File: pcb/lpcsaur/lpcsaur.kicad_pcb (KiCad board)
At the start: 4 copper layers, 116.8 x 71.1 mm, 157 parts, among them IC1 74LV11, IC2 74LV10, IC3 74HCT08, IC4 74LVC07, IC5 74LVC07, IC6 LM1117-3.3, IC7 LPC1768_TQFP100, J1 X1, J10 LASER, J11 Motor X, J12 Motor Y, J13 Motor Z, J14 Motor AUX, J15 SSR, J16 SSR AUX, J17 RELAY1, J18 V-SELECT, J19 RELAY2, J2 X2, J20 V-SELECT, J21 USB_B, J22 RGB LED, J23 SERIAL, J24 5V IN, J25 12V IN, J26 24V IN, J27 AUX I/O, J28 CHILLER, J29 MICRO-SD, J3 Y1, J4 Y2, J5 Z1, J6 Z2, J7 DOOR1, J8 DOOR2, J9 E-STOP, P0.0 TEST_1P, P0.1 TEST_1P, Q1 ZXMN4A06, Q2 ZXMN4A06, Q3 BSL207SP, Q4 BSL207SP, SW1 SW_PUSH, SW2 SW_PUSH, SW3 SW_PUSH, X1 12 MHz

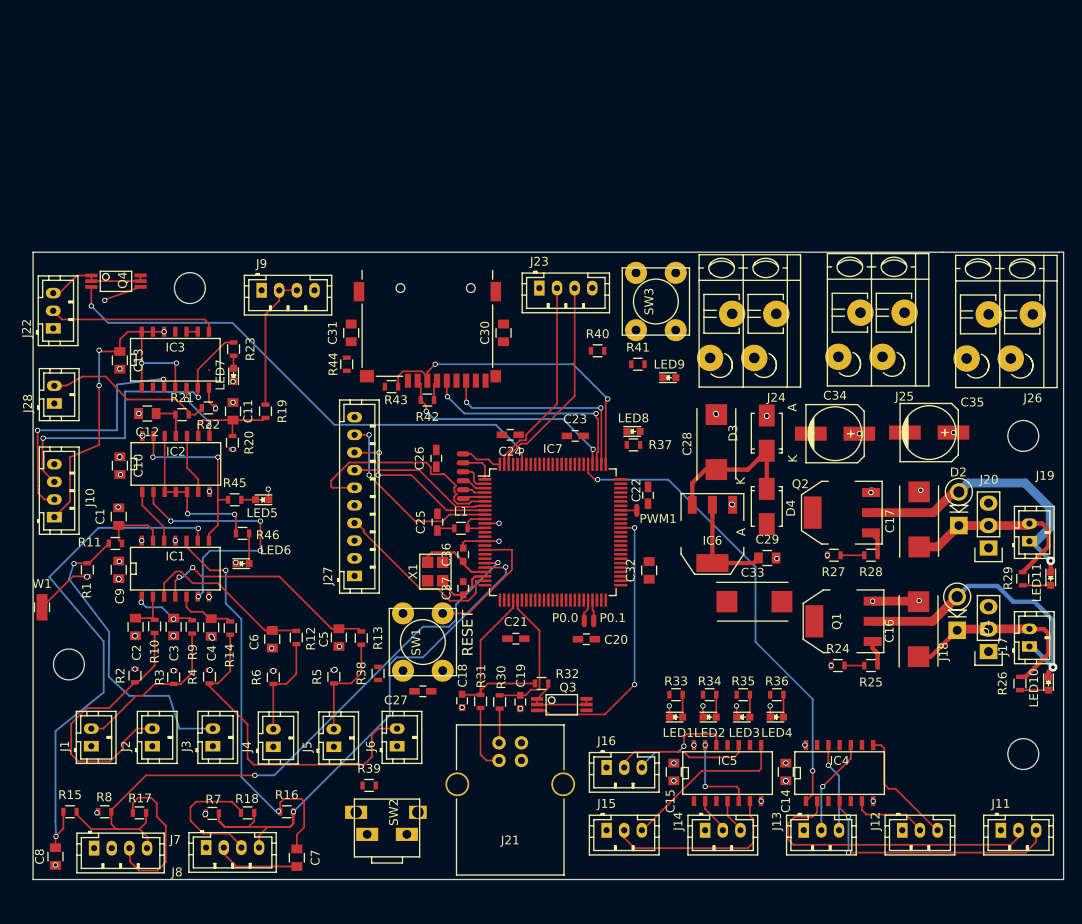
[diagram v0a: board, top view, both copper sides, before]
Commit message: Fix 7410 footprint.
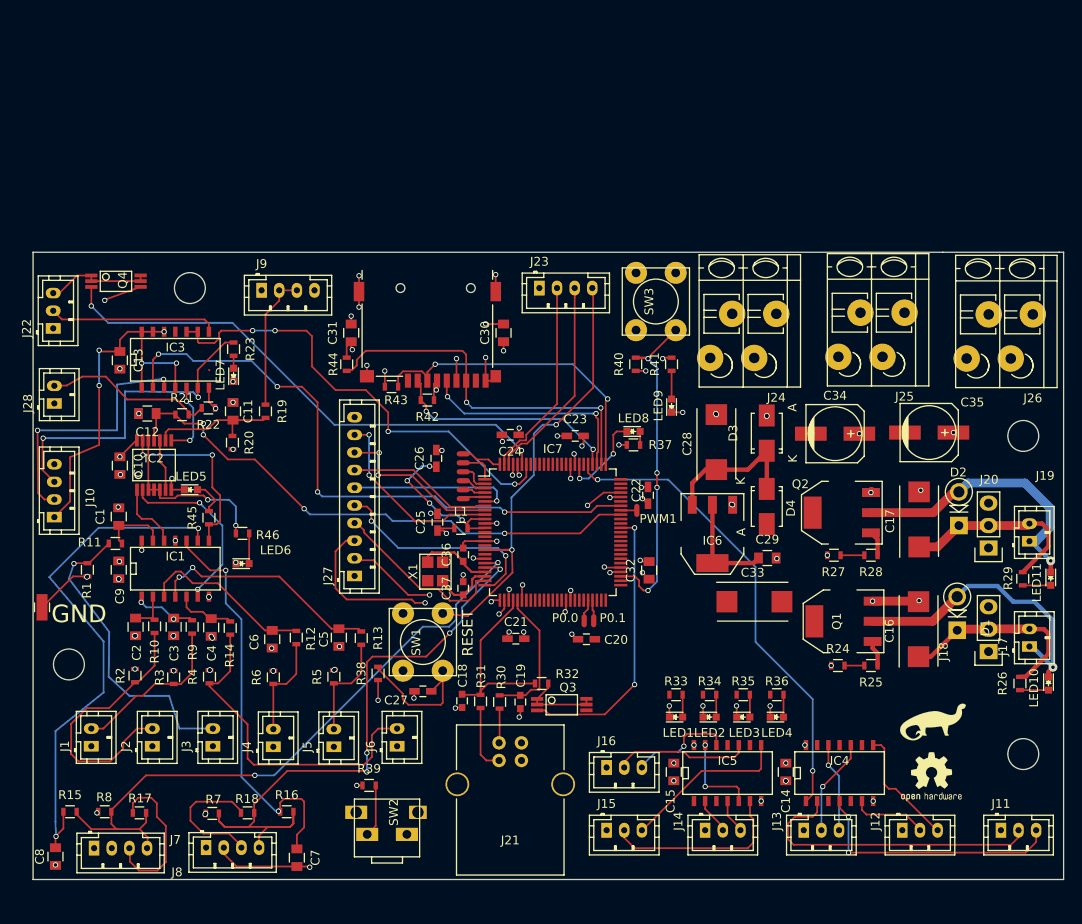
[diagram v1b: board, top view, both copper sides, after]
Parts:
- added G***: LOGO, OPENHARDWARE:OSHWLOGO0.3IN, F.Cu at (186.4, 132.0)
- added G***: LOGO, lpcsaur:dino, F.Cu at (190.1, 129.3)
- IC2: footprint SMD_Packages:SOIC-14_N -> SMD_Packages:SSOP-14
- moved LED5 8.15 mm to (106.3, 103.1), turned to 0 degrees
- moved R40 4.58 mm to (156.7, 88.9), turned to 90 degrees
- moved R41 3.81 mm to (160.8, 88.9), turned to 90 degrees
- moved R45 3.56 mm to (108.3, 106.3), turned to 90 degrees
- moved LED9 3.19 mm to (160.8, 93.6), turned to 90 degrees
- moved IC2 2.49 mm to (102.1, 100.3)
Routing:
- net GND: track 481.3 -> 771.3 mm, vias 63 -> 87
- net +3V3: track 159.4 -> 355.8 mm, vias 12 -> 32
- net +5V: track 140.7 -> 259.1 mm
- net PWM0: track 0.00 -> 70.1 mm, vias 0 -> 4
- net P2.6: track 4.67 -> 63.2 mm, vias 0 -> 4
- net ~RESET: track 15.2 -> 69.4 mm, vias 0 -> 2
- net P1.1: track 1.27 -> 52.9 mm, vias 0 -> 4
- net ~ISP: track 0.00 -> 38.5 mm, vias 0 -> 4
- net Net-(IC7-Pad27): track 0.00 -> 28.7 mm, vias 0 -> 2
- net Net-(IC7-Pad25): track 0.00 -> 25.1 mm, vias 0 -> 2
- net Net-(IC7-Pad26): track 0.00 -> 18.6 mm, vias 0 -> 2
- net SD_MISO: track 24.4 -> 42.4 mm
- net Net-(C26-Pad1): track 4.79 -> 18.1 mm, vias 0 -> 4
- net PLAY_LED: track 0.00 -> 10.4 mm, vias 0 -> 2
- net Net-(IC1-Pad6): track 29.2 -> 20.5 mm, vias 4 -> 2
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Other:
- board text added: "GND"

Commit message: Complete routing.
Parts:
- removed P0.0, P0.1: TEST_1P, lpcsaur2:TP_Oblong
- renumbered Hole2 to Hole4
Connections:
- IC3 pad 11: Net-(IC3-Pad11) -> (no net)
- IC7 pad 13: Net-(IC7-Pad13) -> (no net)
- IC7 pad 14: Net-(IC7-Pad14) -> (no net)
- IC7 pad 16: Net-(IC7-Pad16) -> (no net)
- IC7 pad 18: Net-(IC7-Pad18) -> (no net)
- IC7 pad 46: Net-(IC7-Pad46) -> (no net)
- IC7 pad 47: Net-(IC7-Pad47) -> (no net)
- IC7 pad 48: Net-(IC7-Pad48) -> (no net)
- IC7 pad 50: Net-(IC7-Pad50) -> (no net)
- IC7 pad 52: Net-(IC7-Pad52) -> (no net)
- IC7 pad 57: Net-(IC7-Pad57) -> (no net)
- IC7 pad 62: Net-(IC7-Pad62) -> (no net)
- IC7 pad 65: Net-(IC7-Pad65) -> (no net)
- IC7 pad 66: Net-(IC7-Pad66) -> (no net)
- IC7 pad 81: Net-(IC7-Pad81) -> (no net)
- IC7 pad 85: Net-(IC7-Pad85) -> (no net)
- IC7 pad 86: Net-(IC7-Pad86) -> (no net)
- IC7 pad 87: Net-(IC7-Pad87) -> (no net)
- IC7 pad 88: Net-(IC7-Pad88) -> (no net)
- IC7 pad 89: Net-(IC7-Pad89) -> (no net)
- IC7 pad 90: Net-(IC7-Pad90) -> (no net)
- IC7 pad 91: Net-(IC7-Pad91) -> (no net)
- IC7 pad 92: Net-(IC7-Pad92) -> (no net)
- IC7 pad 93: Net-(IC7-Pad93) -> (no net)
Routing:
- net LED4: track 0.00 -> 136.2 mm, vias 0 -> 8
- net X-MAX: track 30.8 -> 114.3 mm, vias 0 -> 8
- net P1.22: track 2.25 -> 85.7 mm, vias 0 -> 6
- net Y-MIN: track 34.7 -> 98.2 mm, vias 1 -> 3
- net STEP1: track 0.00 -> 63.2 mm, vias 0 -> 2
- net P1.23: track 2.69 -> 62.2 mm, vias 0 -> 6
- net X-MIN: track 18.5 -> 73.2 mm, vias 0 -> 6
- net DIR2: track 0.00 -> 53.5 mm, vias 0 -> 2
- net STEP4: track 0.00 -> 53.0 mm, vias 0 -> 5
- net STEP2: track 0.00 -> 52.2 mm
- net STEP3: track 0.00 -> 49.3 mm, vias 0 -> 2
- net PLAY: track 5.95 -> 54.6 mm, vias 0 -> 8
- net V_USB: track 0.00 -> 48.0 mm, vias 0 -> 5
- net DIR4: track 0.00 -> 45.0 mm, vias 0 -> 7
- net +3V3: track 355.8 -> 400.7 mm, vias 32 -> 34
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
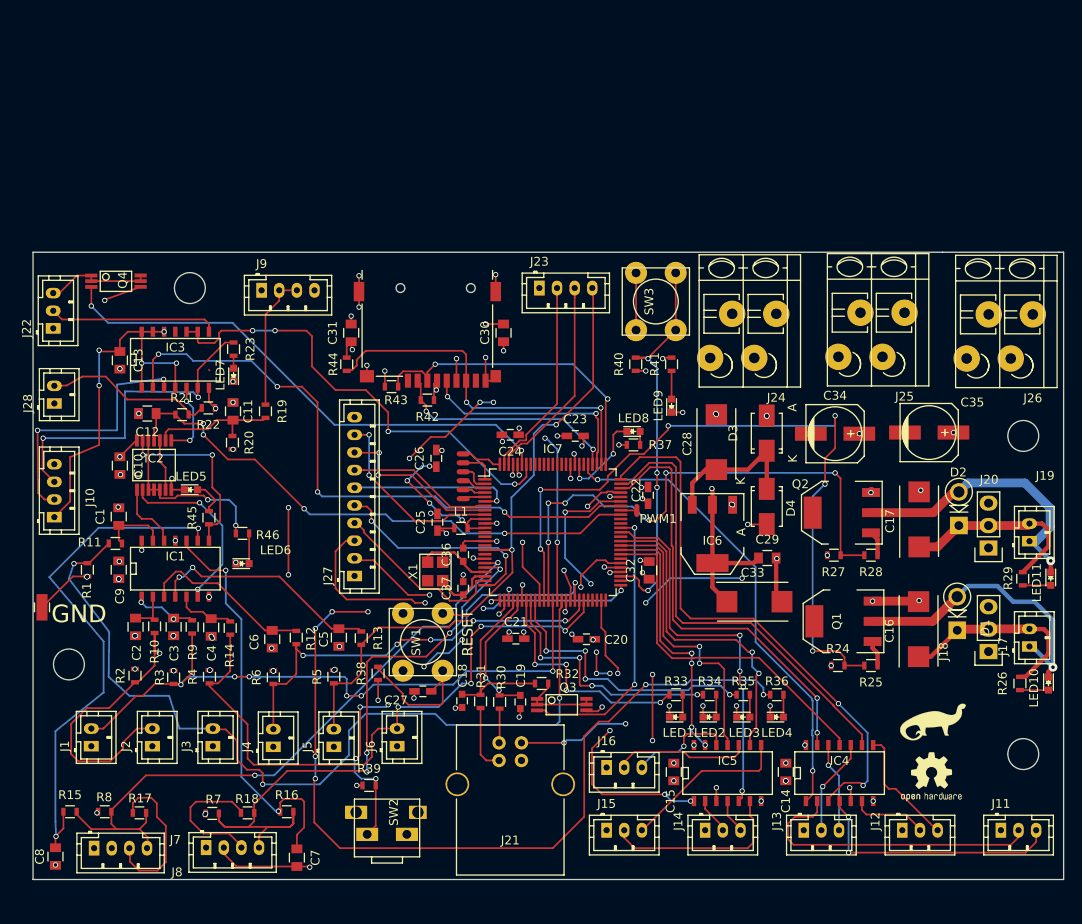
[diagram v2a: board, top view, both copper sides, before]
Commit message: Add ground/power fill. Fix labels.
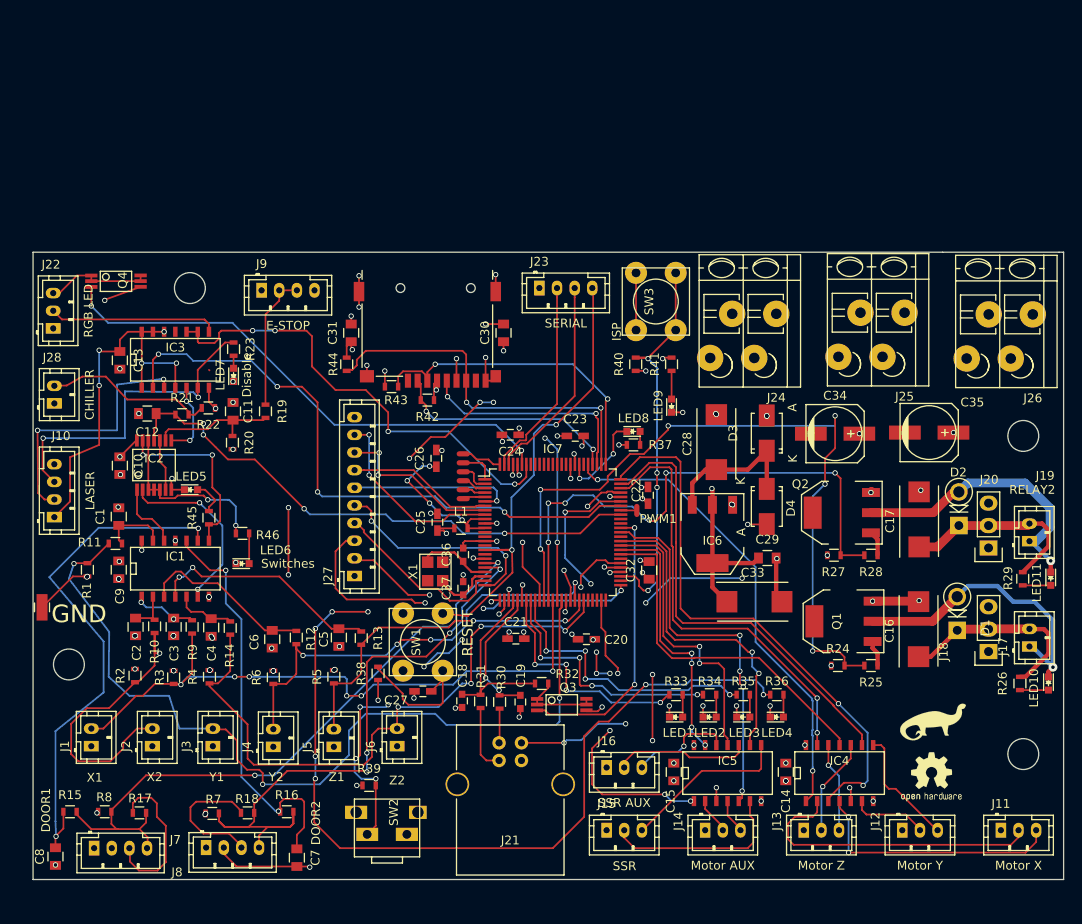
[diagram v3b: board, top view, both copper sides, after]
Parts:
- SW3: value SW_PUSH -> ISP
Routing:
- added copper zone on In1.Cu, net +3V3
- added copper zone on In2.Cu, net GND
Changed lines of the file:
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@@
   (general
     (links 367)
-    (no_connects 1)
+    (no_connects 0)
     (area 84.152429 70.638999 208.963572 147.5695)
     (thickness 1.6)
@@
     (visible_elements FFFFEF7F)
     (pcbplotparams
-      (layerselection 0x010f0_80000007)
+      (layerselection 0x210f0_80000007)
       (usegerberextensions true)
       (excludeedgelayer true)
@@
       (drillshape 0)
       (scaleselection 1)
-      (outputdirectory protel/))
+      (outputdirectory gerber/protel/))
   )
   (net 0 "")
@@
       (effects (font (size 1 1) (thickness 0.15)))
     )
-    (fp_text value X1 (at -3.556 0.381 180) (layer F.Fab)
+    (fp_text value X1 (at -3.556 0.381 180) (layer F.SilkS)
       (effects (font (size 1 1) (thickness 0.15)))
     )
@@
       (effects (font (size 1 1) (thickness 0.15)))
     )
-    (fp_text value X2 (at -3.4925 0.254 180) (layer F.Fab)
+    (fp_text value X2 (at -3.4925 0.254 180) (layer F.SilkS)
       (effects (font (size 1 1) (thickness 0.15)))
     )
@@
       (effects (font (size 1 1) (thickness 0.15)))
     )
-    (fp_text value Y1 (at -3.4925 0.4445 180) (layer F.Fab)
+    (fp_text value Y1 (at -3.4925 0.4445 180) (layer F.SilkS)
       (effects (font (size 1 1) (thickness 0.15)))
     )
@@
       (effects (font (size 1 1) (thickness 0.15)))
     )
-    (fp_text value Y2 (at -3.429 0.3175 180) (layer F.Fab)
+    (fp_text value Y2 (at -3.429 0.3175 180) (layer F.SilkS)
       (effects (font (size 1 1) (thickness 0.15)))
     )
@@
       (effects (font (size 1 1) (thickness 0.15)))
     )
-    (fp_text value Z1 (at -3.429 0.3175 180) (layer F.Fab)
+    (fp_text value Z1 (at -3.429 0.3175 180) (layer F.SilkS)
       (effects (font (size 1 1) (thickness 0.15)))
     )
@@
       (effects (font (size 1 1) (thickness 0.15)))
     )
-    (fp_text value Z2 (at -3.8735 0 180) (layer F.Fab)
+    (fp_text value Z2 (at -3.8735 0 180) (layer F.SilkS)
       (effects (font (size 1 1) (thickness 0.15)))
     )
@@
       (effects (font (size 1 1) (thickness 0.15)))
     )
-    (fp_text value DOOR1 (at -5.461 -4.318 90) (layer F.Fab)
+    (fp_text value DOOR1 (at -5.461 -4.318 90) (layer F.SilkS)
       (effects (font (size 1 1) (thickness 0.15)))
     )
@@
       (effects (font (size 1 1) (thickness 0.15)))
     )
-    (fp_text value DOOR2 (at 12.446 -2.794 90) (layer F.Fab)
+    (fp_text value DOOR2 (at 12.446 -2.794 90) (layer F.SilkS)
       (effects (font (size 1 1) (thickness 0.15)))
     )
@@
       (effects (font (size 1 1) (thickness 0.15)))
     )
-    (fp_text value E-STOP (at 3 4) (layer F.Fab)
+    (fp_text value E-STOP (at 3 4) (layer F.SilkS)
       (effects (font (size 1 1) (thickness 0.15)))
     )
@@
     (descr http://www.jst-mfg.com/product/pdf/eng/ePH.pdf)
     (tags "connector jst ph")
-    (fp_text reference J10 (at 2.2225 4.064 90) (layer F.SilkS)
+    (fp_text reference J10 (at 9.2075 0.762 180) (layer F.SilkS)
       (effects (font (size 1 1) (thickness 0.15)))
     )
-    (fp_text value LASER (at -3.2385 0 180) (layer F.Fab)
+    (fp_text value LASER (at 2.9845 4.064 270) (layer F.SilkS)
       (effects (font (size 1 1) (thickness 0.15)))
     )
@@
       (effects (font (size 1 1) (thickness 0.15)))
     )
-    (fp_text value "Motor X" (at 2 4) (layer F.Fab)
+    (fp_text value "Motor X" (at 2 4) (layer F.SilkS)
       (effects (font (size 1 1) (thickness 0.15)))
     )
@@
       (effects (font (size 1 1) (thickness 0.15)))
     )
-    (fp_text value "Motor Y" (at 2 4) (layer F.Fab)
+    (fp_text value "Motor Y" (at 2 4) (layer F.SilkS)
       (effects (font (size 1 1) (thickness 0.15)))
     )
@@
       (effects (font (size 1 1) (thickness 0.15)))
     )
-    (fp_text value "Motor Z" (at 2 4) (layer F.Fab)
+    (fp_text value "Motor Z" (at 2 4) (layer F.SilkS)
       (effects (font (size 1 1) (thickness 0.15)))
     )
@@
       (effects (font (size 1 1) (thickness 0.15)))
     )
-    (fp_text value "Motor AUX" (at 2 4) (layer F.Fab)
+    (fp_text value "Motor AUX" (at 2 4) (layer F.SilkS)
       (effects (font (size 1 1) (thickness 0.15)))
     )
@@
       (effects (font (size 1 1) (thickness 0.15)))
     )
-    (fp_text value SSR (at 2.032 4.064 180) (layer F.Fab)
+    (fp_text value SSR (at 2.032 4.064) (layer F.SilkS)
       (effects (font (size 1 1) (thickness 0.15)))
     )
@@
       (effects (font (size 1 1) (thickness 0.15)))
     )
-    (fp_text value "SSR AUX" (at 2 4) (layer F.Fab)
+    (fp_text value "SSR AUX" (at 2 4) (layer F.SilkS)
       (effects (font (size 1 1) (thickness 0.15)))
     )
@@
       (effects (font (size 1 1) (thickness 0.15)))
     )
-    (fp_text value RELAY1 (at 5.5245 0.4445 180) (layer F.Fab)
-      (effects (font (size 1 1) (thickness 0.15)))
+    (fp_text value RELAY1 (at 5.5245 0.4445 180) (layer B.SilkS)
+      (effects (font (size 1 1) (thickness 0.15)) (justify mirror))
     )
     (fp_line (start -1.95 2.8) (end -1.95 -1.7) (layer F.SilkS) (width 0.15))
@@
       (effects (font (size 1 1) (thickness 0.15)))
     )
-    (fp_text value RELAY2 (at 5.842 0.3175 180) (layer F.Fab)
+    (fp_text value RELAY2 (at 5.842 0.3175 180) (layer F.SilkS)
       (effects (font (size 1 1) (thickness 0.15)))
     )
@@
     (descr http://www.jst-mfg.com/product/pdf/eng/ePH.pdf)
     (tags "connector jst ph")
-    (fp_text reference J22 (at 0 -3 90) (layer F.SilkS)
+    (fp_text reference J22 (at 7.239 -0.254 180) (layer F.SilkS)
       (effects (font (size 1 1) (thickness 0.15)))
     )
-    (fp_text value "RGB LED" (at 2 4 90) (layer F.Fab)
+    (fp_text value "RGB LED" (at 2 4 90) (layer F.SilkS)
       (effects (font (size 1 1) (thickness 0.15)))
     )
@@
       (effects (font (size 1 1) (thickness 0.15)))
     )
-    (fp_text value SERIAL (at 3 4) (layer F.Fab)
+    (fp_text value SERIAL (at 3 4) (layer F.SilkS)
       (effects (font (size 1 1) (thickness 0.15)))
     )
@@
     (descr http://www.jst-mfg.com/product/pdf/eng/ePH.pdf)
     (tags "connector jst ph")
-    (fp_text reference J28 (at 0 -3 90) (layer F.SilkS)
+    (fp_text reference J28 (at 5.207 -0.254 180) (layer F.SilkS)
       (effects (font (size 1 1) (thickness 0.15)))
     )
-    (fp_text value CHILLER (at 1 4 90) (layer F.Fab)
+    (fp_text value CHILLER (at 1 4 90) (layer F.SilkS)
       (effects (font (size 1 1) (thickness 0.15)))
     )
@@
       (effects (font (size 1 1) (thickness 0.15)))
     )
-    (fp_text value Switches (at 5.1435 0) (layer F.Fab)
+    (fp_text value Switches (at 5.1435 0) (layer F.SilkS)
       (effects (font (size 1 1) (thickness 0.15)))
     )
@@
       (effects (font (size 1 1) (thickness 0.15)))
     )
-    (fp_text value Disable (at 0 1.5 90) (layer F.Fab)
+    (fp_text value Disable (at 0 1.5 90) (layer F.SilkS)
       (effects (font (size 1 1) (thickness 0.15)))
     )
@@
       (effects (font (size 1 1) (thickness 0.15)))
     )
-    (fp_text value SW_PUSH (at 0 1.016 90) (layer F.Fab)
+    (fp_text value ISP (at -3.429 -4.445 90) (layer F.SilkS)
       (effects (font (size 1 1) (thickness 0.15)))
     )
@@
   (via (at 163.068 122.809) (size 0.6) (drill 0.4) (layers F.Cu B.Cu) (net 123))
   (via (at 163.068 121.666) (size 0.6) (drill 0.4) (layers F.Cu B.Cu) (net 123))
+  (zone (net 2) (net_name GND) (layer In2.Cu) (hatch edge 0.508)
+    (connect_pads (clearance 0.508))
+    (min_thickness 0.254)
+    (fill yes (arc_segments 16) (thermal_gap 0.508) (thermal_bridge_width 0.508))
+    (polygon
+      (pts
+        (xy 88.773 76.454) (xy 204.978 76.454) (xy 204.978 147.066) (xy 88.646 147.066) (xy 88.519 76.454)
+      )
+    )
+  )
+  (zone (net 10) (net_name +3V3) (layer In1.Cu) (hatch edge 0.508)
+    (connect_pads (clearance 0.508))
+    (min_thickness 0.254)
+    (fill yes (arc_segments 16) (thermal_gap 0.508) (thermal_bridge_width 0.508))
+    (polygon
+      (pts
+        (xy 88.773 76.581) (xy 204.978 76.581) (xy 204.851 146.812) (xy 88.646 147.066) (xy 88.646 76.581)
+      )
+    )
+  )
 )
